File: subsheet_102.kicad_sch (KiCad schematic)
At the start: 24 parts

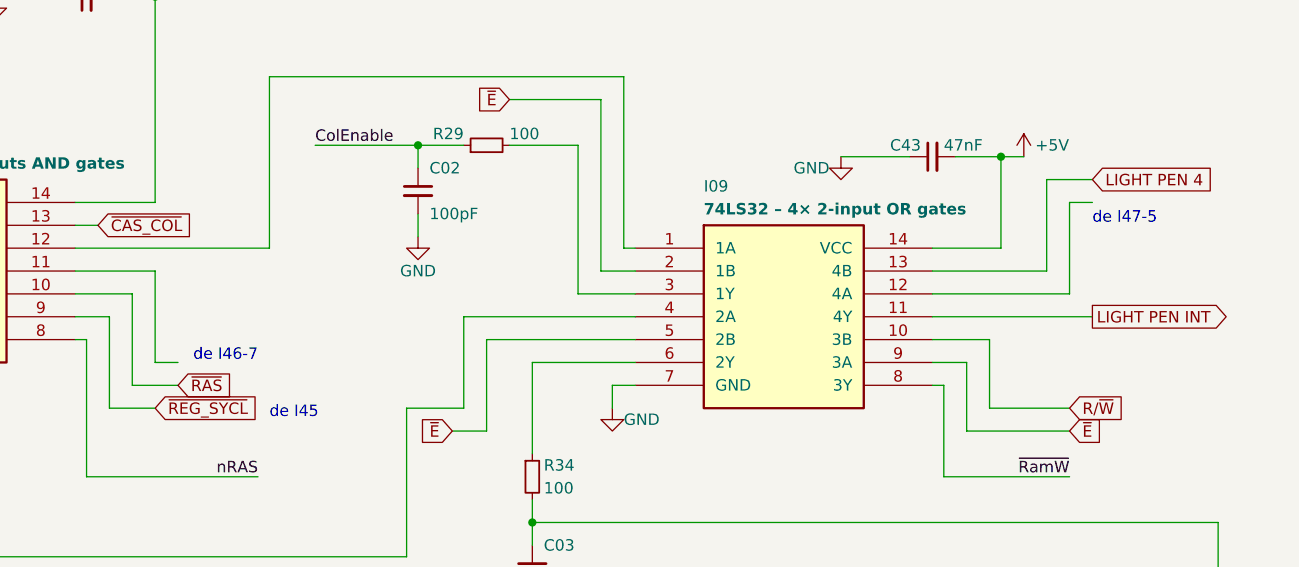
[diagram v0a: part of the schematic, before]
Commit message: Nommage de signaux d'après documentations techniques
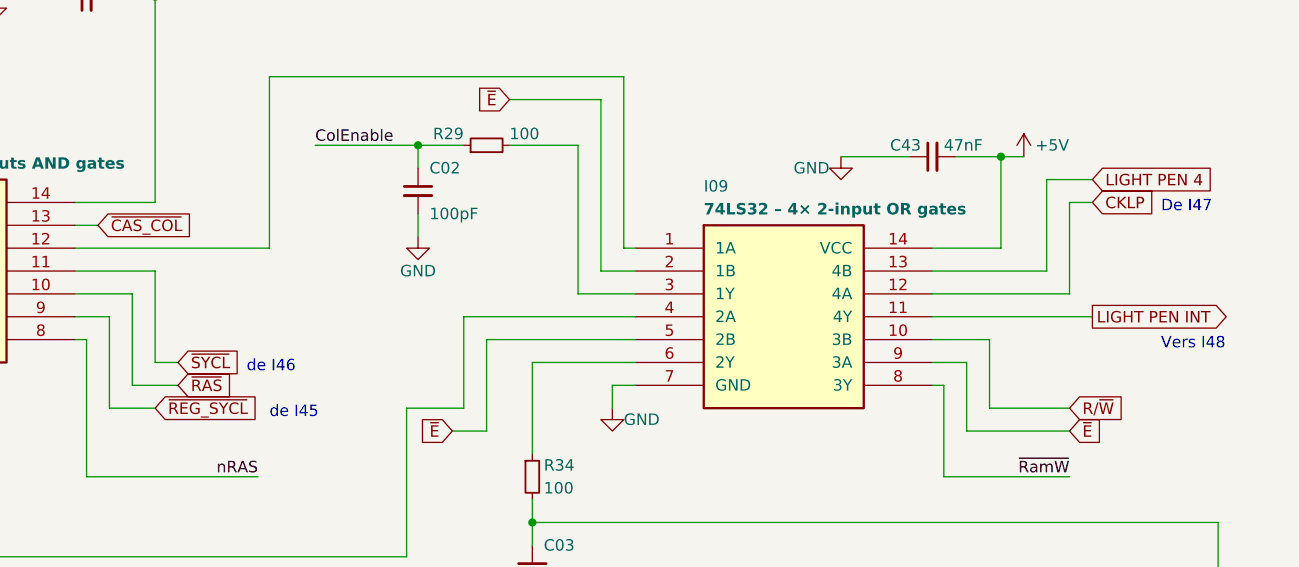
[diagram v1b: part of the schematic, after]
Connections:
- net ~{SYCL}: now reaches I12.11 (3C)
- net CKLP: now reaches I09.12 (4A)
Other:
- note added: "De I47"
- note added: "Vers I48"
- note added: "de I46"
- note removed: "de I46-7"
- note removed: "de I47-5"
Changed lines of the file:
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@@
     (effects (font (size 2.54 2.54)) (justify left bottom))
   )
+  (text "Vers I48" (at 187.96 77.47 0)
+    (effects (font (size 1.27 1.27)) (justify left bottom))
+  )
   (text "de I45" (at 88.9 85.09 0)
     (effects (font (size 1.27 1.27)) (justify left bottom))
   )
-  (text "de I47-5" (at 180.34 63.5 0)
+  (text "De I47" (at 187.96 62.23 0)
     (effects (font (size 1.27 1.27)) (justify left bottom))
   )
@@
     (effects (font (size 2.54 2.54)) (justify left bottom))
   )
-  (text "de I46-7" (at 87.63 78.74 180)
-    (effects (font (size 1.27 1.27)) (justify right bottom))
+  (text "de I46" (at 86.36 80.01 0)
+    (effects (font (size 1.27 1.27)) (justify left bottom))
   )
   (text "Point" (at 160.02 247.65 0)
@@
     )
   )
+  (global_label "~{SYCL}" (shape input) (at 78.74 78.74 0) (fields_autoplaced)
+    (effects (font (size 1.27 1.27)) (justify left))
+    (property "Intersheet References" "${INTERSHEET_REFS}" (id 0) (at 85.7493 78.6606 0)
+      (effects (font (size 1.27 1.27)) (justify left) hide)
+    )
+  )
   (global_label "R{slash}~{W}" (shape input) (at 143.51 127 180) (fields_autoplaced)
     (effects (font (size 1.27 1.27)) (justify right))
@@
       (effects (font (size 1.27 1.27)) (justify left) hide)
     )
+  )
+  (global_label "CKLP" (shape input) (at 180.34 60.96 0) (fields_autoplaced)
+    (effects (font (size 1.27 1.27)) (justify left))
+    (property "Intersheet References" "${INTERSHEET_REFS}" (id 0) (at 187.5912 60.8806 0)
+      (effects (font (size 1.27 1.27)) (justify left) hide)
+    )
